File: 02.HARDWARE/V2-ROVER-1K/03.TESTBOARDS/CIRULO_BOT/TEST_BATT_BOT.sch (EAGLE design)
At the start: 6 parts

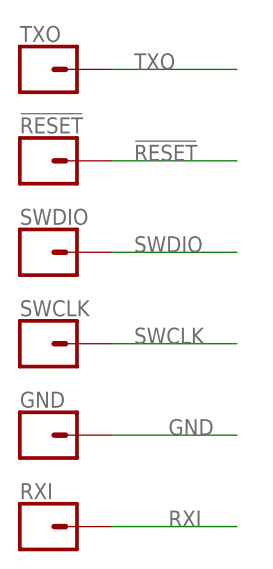
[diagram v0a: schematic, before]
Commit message: Versiones v2 pendientes de revision de conjunto de PCBs Cirulo programacion.
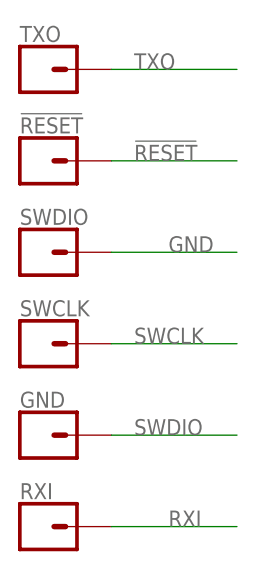
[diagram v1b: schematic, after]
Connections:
- net GND: now also SWDIO.1; no longer GND.1
- net SWDIO: now also GND.1; no longer SWDIO.1
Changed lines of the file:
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@@
 <drawing>
 <settings>
-<setting alwaysvectorfont="no"/>
+<setting alwaysvectorfont="yes"/>
 <setting verticaltext="up"/>
 </settings>
@@
 </segment>
 </net>
-<net name="SWDIO" class="0">
-<segment>
-<label x="82.55" y="66.04" size="1.778" layer="95"/>
-<pinref part="SWDIO" gate="G$1" pin="1"/>
-<wire x1="80.01" y1="66.04" x2="93.98" y2="66.04" width="0.1524" layer="91"/>
-</segment>
-</net>
 <net name="TXO" class="0">
 <segment>
@@
 </segment>
 </net>
-<net name="GND" class="0">
-<segment>
-<pinref part="GND" gate="G$1" pin="1"/>
-<wire x1="80.01" y1="45.72" x2="93.98" y2="45.72" width="0.1524" layer="91"/>
-<label x="86.36" y="45.72" size="1.778" layer="95"/>
-</segment>
-</net>
 <net name="RXI" class="0">
 <segment>
@@
 </segment>
 </net>
+<net name="SWDIO" class="0">
+<segment>
+<label x="82.55" y="45.72" size="1.778" layer="95"/>
+<wire x1="80.01" y1="45.72" x2="93.98" y2="45.72" width="0.1524" layer="91"/>
+<pinref part="GND" gate="G$1" pin="1"/>
+</segment>
+</net>
+<net name="GND" class="0">
+<segment>
+<wire x1="80.01" y1="66.04" x2="93.98" y2="66.04" width="0.1524" layer="91"/>
+<label x="86.36" y="66.04" size="1.778" layer="95"/>
+<pinref part="SWDIO" gate="G$1" pin="1"/>
+</segment>
+</net>
